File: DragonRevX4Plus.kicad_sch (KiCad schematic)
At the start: 14 parts, among them J14 PWR_LED, J15 PWR_SWITCH, J7 COMPOSITE

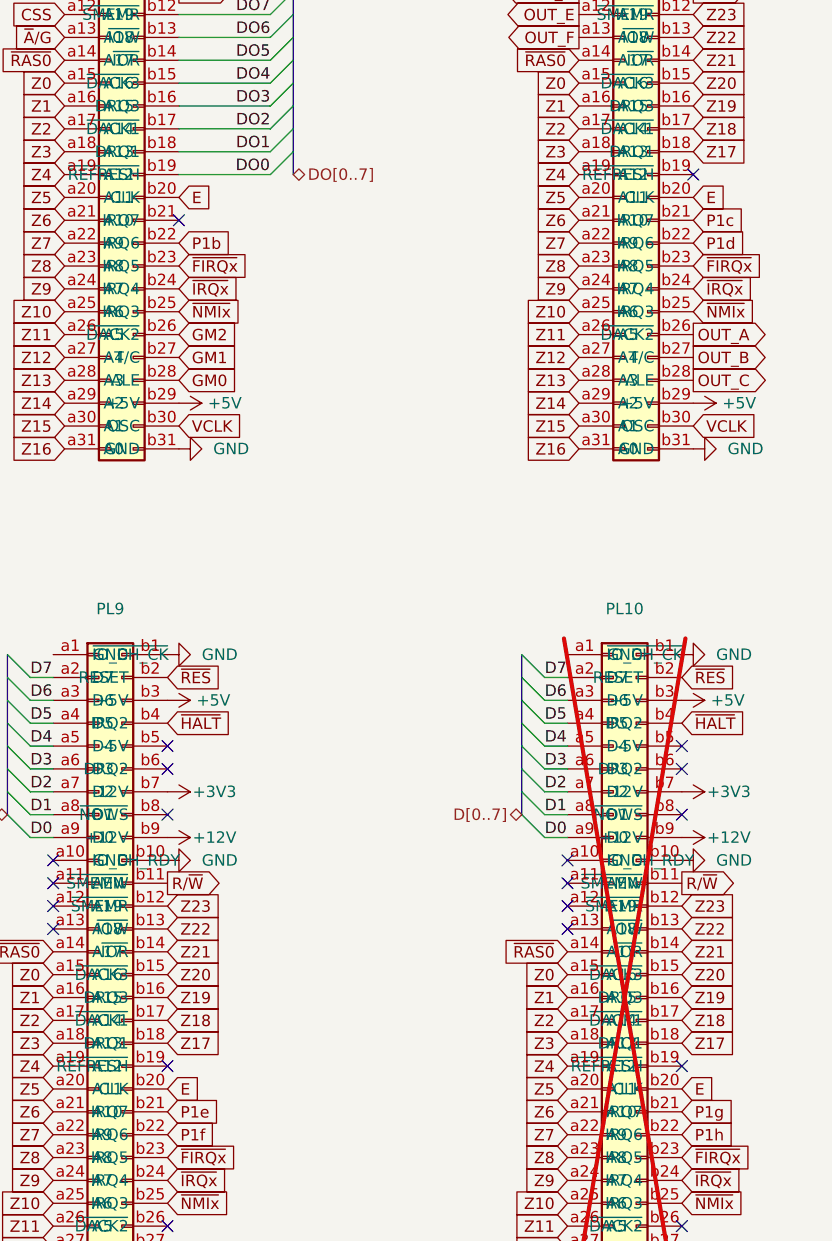
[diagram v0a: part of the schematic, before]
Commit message: fix missing Q signal to expansion ports
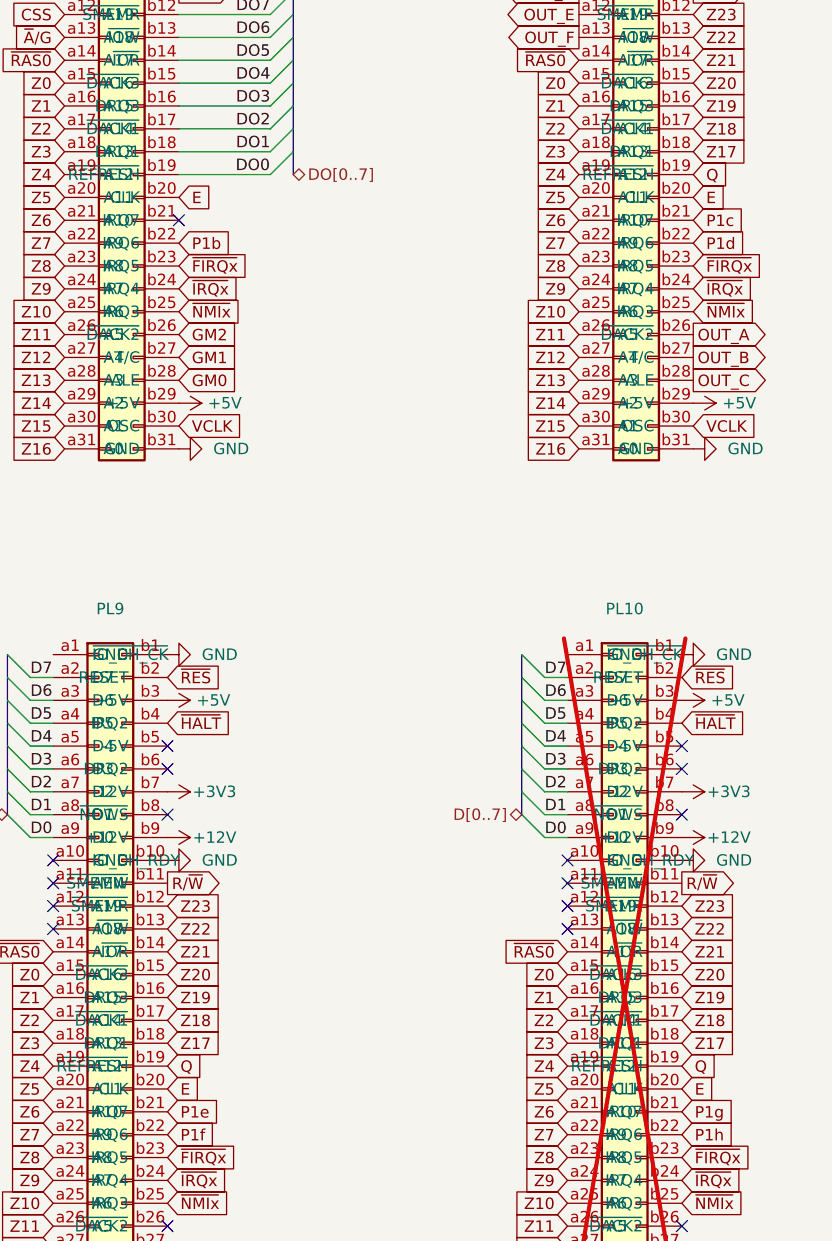
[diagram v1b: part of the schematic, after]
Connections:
- net Q: now reaches PL10.b19 (~{REFRESH})
- net Q: now also PL4.b19 (~{REFRESH}), PL9.b19 (~{REFRESH})
- no-connect marks 33 -> 30
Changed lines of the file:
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@@
 	)
 	(no_connect
-		(at 316.23 170.18)
-	)
-	(no_connect
 		(at 374.65 38.1)
 	)
@@
 	)
 	(no_connect
-		(at 374.65 71.12)
-	)
-	(no_connect
 		(at 196.85 44.45)
 	)
@@
 	)
 	(no_connect
-		(at 373.38 170.18)
-	)
-	(no_connect
 		(at 317.5 35.56)
 	)
@@
 		)
 	)
+	(global_label "Q"
+		(shape input)
+		(at 373.38 170.18 0)
+		(fields_autoplaced yes)
+		(effects
+			(font
+				(size 1.27 1.27)
+			)
+			(justify left)
+		)
+		(property "Intersheetrefs" "${INTERSHEET_REFS}"
+			(at 377.6957 170.18 0)
+			(effects
+				(font
+					(size 1.27 1.27)
+				)
+				(justify left)
+				(hide yes)
+			)
+		)
+	)
 	(global_label "Z2"
 		(shape input)
@@
 		)
 	)
+	(global_label "Q"
+		(shape input)
+		(at 316.23 170.18 0)
+		(fields_autoplaced yes)
+		(effects
+			(font
+				(size 1.27 1.27)
+			)
+			(justify left)
+		)
+		(property "Intersheetrefs" "${INTERSHEET_REFS}"
+			(at 320.5457 170.18 0)
+			(effects
+				(font
+					(size 1.27 1.27)
+				)
+				(justify left)
+				(hide yes)
+			)
+		)
+	)
 	(global_label "VCLK"
 		(shape input)
@@
 				(hide yes)
 			)
+		)
+	)
+	(global_label "Q"
+		(shape input)
+		(at 374.65 71.12 0)
+		(fields_autoplaced yes)
+		(effects
+			(font
+				(size 1.27 1.27)
+			)
+			(justify left)
+		)
+		(property "Intersheetrefs" "${INTERSHEET_REFS}"
+			(at 378.9657 71.12 0)
+			(effects
+				(font
+					(size 1.27 1.27)
+				)
+				(justify left)
+				(hide yes)
+			)

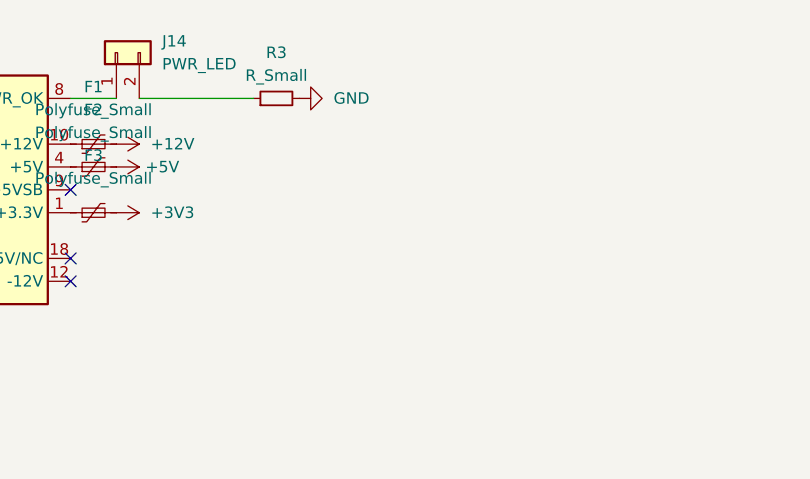
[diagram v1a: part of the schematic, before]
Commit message: route data bus to sam
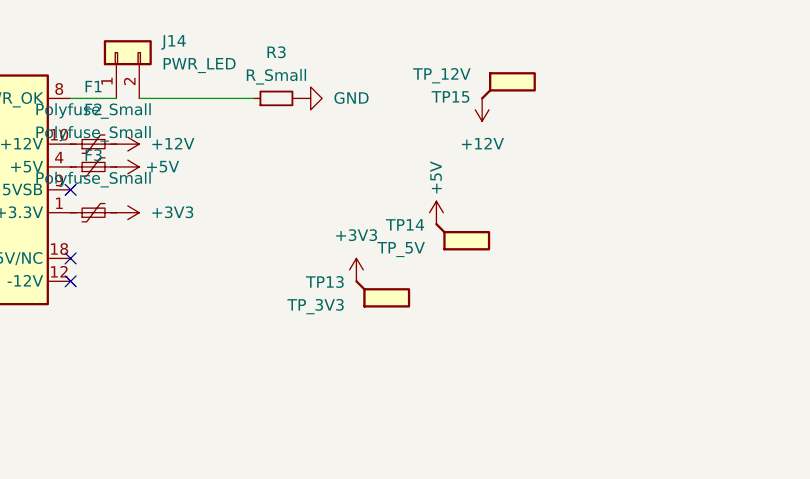
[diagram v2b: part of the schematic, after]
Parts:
- added TP13: TP_3V3, TestPoint:TestPoint_Loop_D1.80mm_Drill1.0mm_Beaded, symbol Connector:TestPoint_Flag
- added TP14: TP_5V, TestPoint:TestPoint_Loop_D1.80mm_Drill1.0mm_Beaded, symbol Connector:TestPoint_Flag
- added TP15: TP_12V, TestPoint:TestPoint_Loop_D1.80mm_Drill1.0mm_Beaded, symbol Connector:TestPoint_Flag
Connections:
- net +12V: now also TP15.1
- net +3V3: now also TP13.1
- net +5V: now also TP14.1

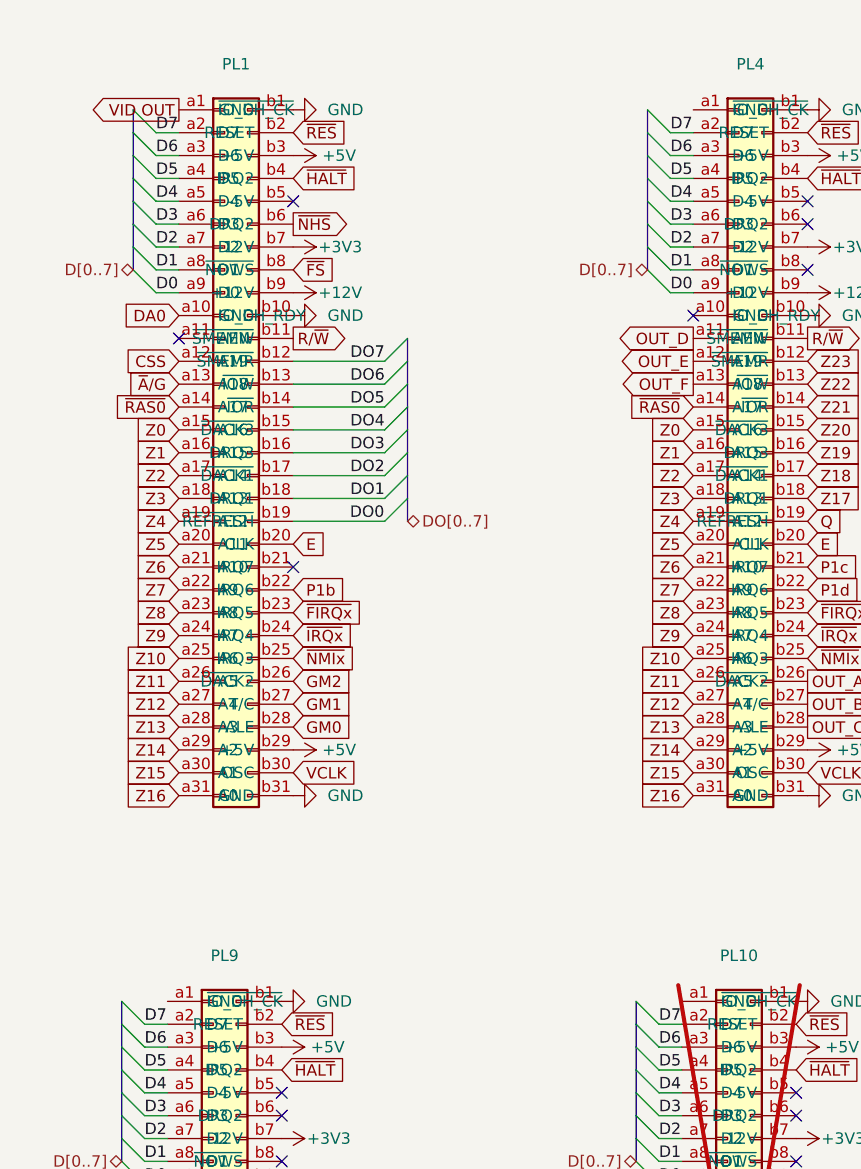
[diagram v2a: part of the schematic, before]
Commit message: update vendor specific BOM fields
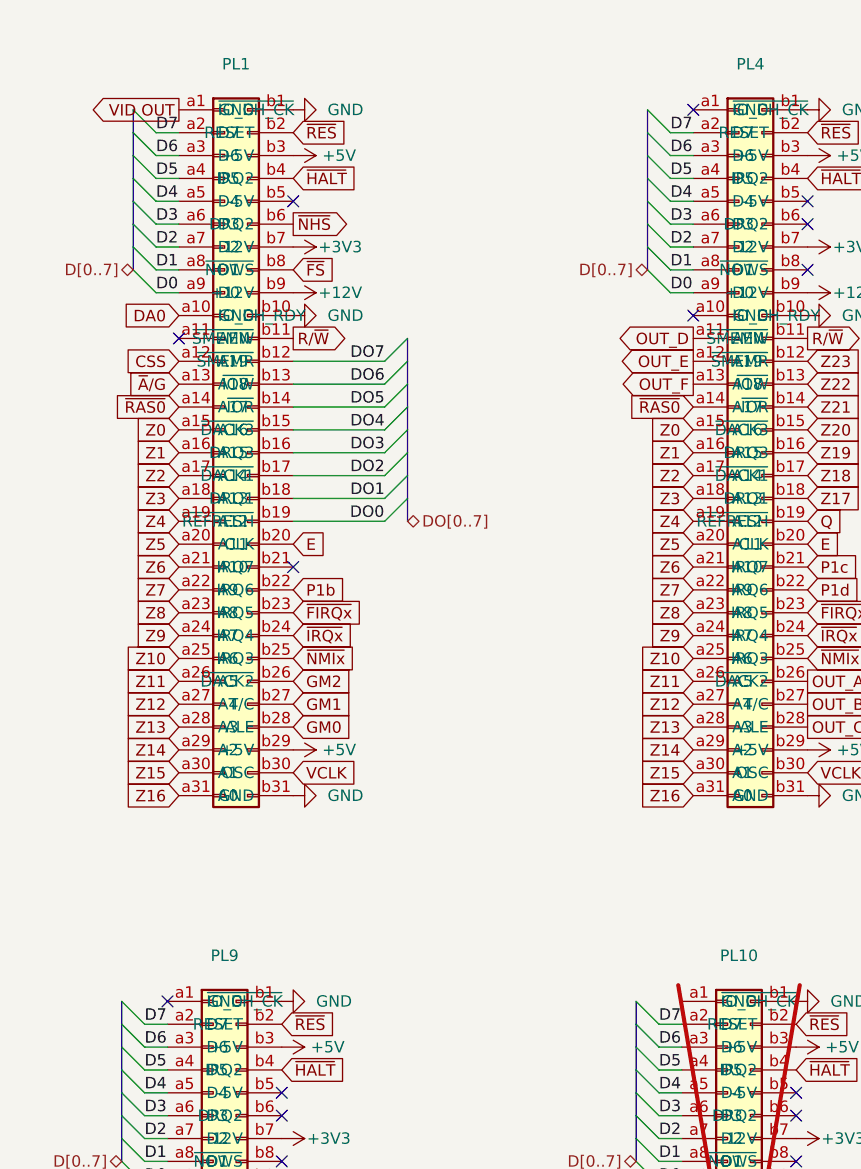
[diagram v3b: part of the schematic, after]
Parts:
- PL1, PL10, PL4, PL9: DigiKey (none) -> EBC31DCWN-S371-ND
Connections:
- no-connect marks 30 -> 32
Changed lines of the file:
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@@
 	)
 	(no_connect
+		(at 303.53 124.46)
+	)
+	(no_connect
 		(at 316.23 187.96)
 	)
@@
 	)
 	(no_connect
+		(at 361.95 25.4)
+	)
+	(no_connect
 		(at 316.23 137.16)
 	)
@@
 			)
 		)
+		(property "DigiKey" "EBC31DCWN-S371-ND"
+			(at 311.15 63.5 0)
+			(effects
+				(font
+					(size 1.27 1.27)
+				)
+				(hide yes)
+			)
+		)
 		(pin "b23"
 		)
@@
 			)
 		)
+		(property "DigiKey" "EBC31DCWN-S371-ND"
+			(at 367.03 162.56 0)
+			(effects
+				(font
+					(size 1.27 1.27)
+				)
+				(hide yes)
+			)
+		)
 		(pin "b23"
 		)
@@
 			)
 		)
+		(property "DigiKey" "EBC31DCWN-S371-ND"
+			(at 309.88 162.56 0)
+			(effects
+				(font
+					(size 1.27 1.27)
+				)
+				(hide yes)
+			)
+		)
 		(pin "b23"
 		)
@@
 			(at 368.3 63.5 0)
 			(effects
+				(font
+					(size 1.27 1.27)
+				)
+				(hide yes)
+			)
+		)
+		(property "DigiKey" "EBC31DCWN-S371-ND"
+			(at 368.3 63.5 0)
+			(effects

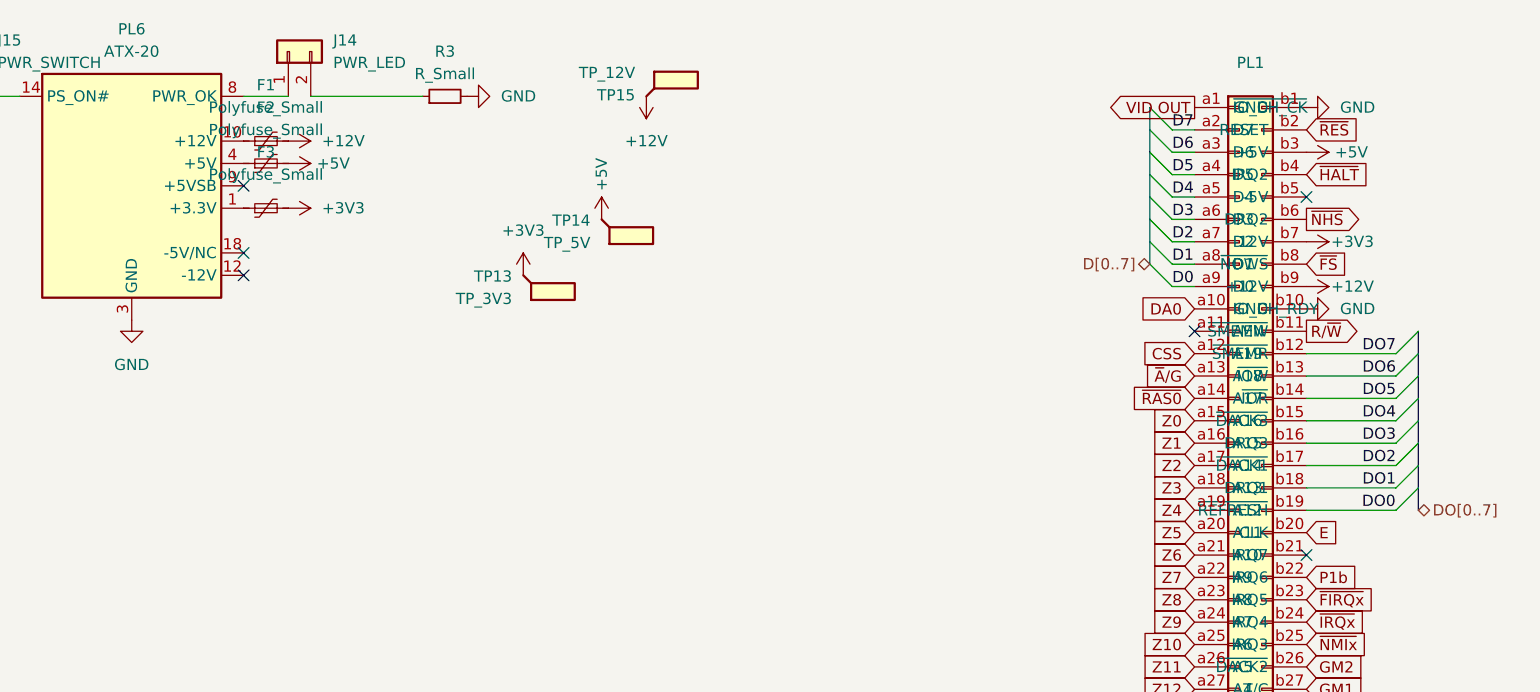
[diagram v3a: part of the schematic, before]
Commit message: update vhdl for correct S and Z operation
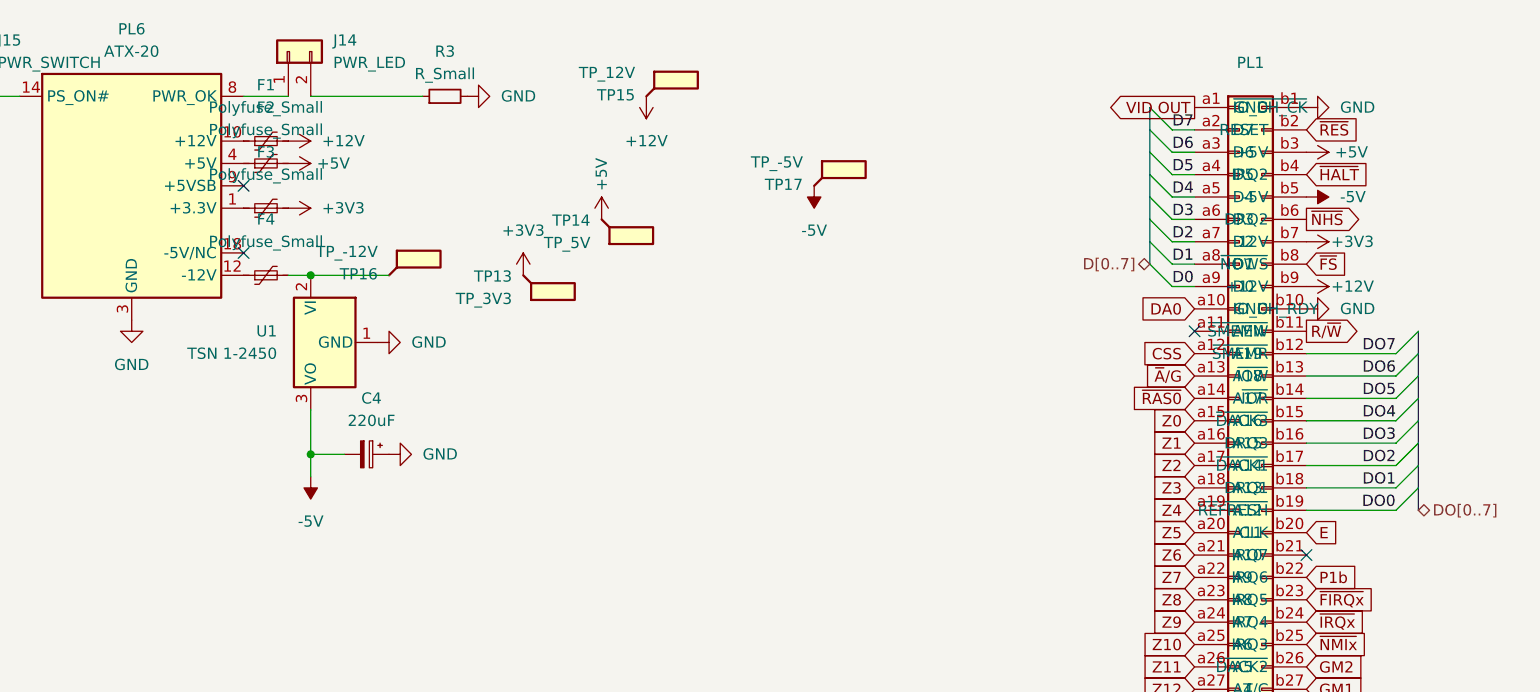
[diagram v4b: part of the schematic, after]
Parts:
- added C4: 220uF, Capacitor_SMD:CP_Elec_6.3x5.4_Nichicon, symbol Device:C_Polarized_Small
- added F4: Polyfuse_Small, Fuse:Fuse_Bourns_MF-RHT400, symbol Device:Polyfuse_Small
- added TP16: TP_-12V, TestPoint:TestPoint_Loop_D1.80mm_Drill1.0mm_Beaded, symbol Connector:TestPoint_Flag
- added TP17: TP_-5V, TestPoint:TestPoint_Loop_D1.80mm_Drill1.0mm_Beaded, symbol Connector:TestPoint_Flag
- added U1: TSN 1-2450, Package_TO_SOT_THT:TO-220-3_Horizontal_TabDown, symbol Regulator_Linear:LM7905_TO220
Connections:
- net GND: now also C4.1, U1.1 (GND)
- net -5V: now reaches PL1.b5 (-5V)
- net -5V: now also C4.2, TP17.1, U1.3 (VO)
- net at PL6.12 (-12V): now also F4.1
- new net: F4.2, TP16.1, U1.2 (VI)
- no-connect marks 32 -> 30
